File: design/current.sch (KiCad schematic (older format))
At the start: 4 parts

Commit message: Starting PIVI 2.0 * sch ready. * components in PCB placed.
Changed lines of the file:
@@
 AR Path="/548DF2C8/55B3BD79/55B231D6" Ref="R35"  Part="1"
 AR Path="/548DF2C8/55B3BD84/55B231D6" Ref="R38"  Part="1"
-F 0 "R23" V 3605 2675 50  0000 C CNN
+F 0 "R38" V 3605 2675 50  0000 C CNN
 F 1 "22R" V 3525 2675 50  0000 C CNN
 F 2 "Resistors_SMD:R_0603" V 3455 2675 30  0001 C CNN
@@
 AR Path="/548DF2C8/55B3BD79/55B23207" Ref="R36"  Part="1"
 AR Path="/548DF2C8/55B3BD84/55B23207" Ref="R39"  Part="1"
-F 0 "R24" V 4080 2675 50  0000 C CNN
+F 0 "R39" V 4080 2675 50  0000 C CNN
 F 1 "10K" V 4000 2675 50  0000 C CNN
 F 2 "Resistors_SMD:R_0603" V 3930 2675 30  0001 C CNN
@@
 AR Path="/548DF2C8/55B3BD79/55B23290" Ref="R37"  Part="1"
 AR Path="/548DF2C8/55B3BD84/55B23290" Ref="R40"  Part="1"
-F 0 "R25" V 4080 3175 50  0000 C CNN
+F 0 "R40" V 4080 3175 50  0000 C CNN
 F 1 "10K" V 4000 3175 50  0000 C CNN
 F 2 "Resistors_SMD:R_0603" V 3930 3175 30  0001 C CNN
@@
 AR Path="/548DF2C8/55B3BD79/55B232D0" Ref="C21"  Part="1"
 AR Path="/548DF2C8/55B3BD84/55B232D0" Ref="C22"  Part="1"
-F 0 "C17" H 3550 3275 50  0000 L CNN
+F 0 "C22" H 3550 3275 50  0000 L CNN
 F 1 "10uF" H 3550 3075 50  0000 L CNN
 F 2 "Capacitors_SMD:C_0805" H 3563 3025 30  0001 C CNN
@@
 Connection ~ 4000 2875
 $Comp
-L GND #PWR52
+L GND #PWR057
 U 1 1 55B23417
 P 3525 3375
-AR Path="/548DF2C8/55B266EE/55B23417" Ref="#PWR52"  Part="1"
-AR Path="/548DF2C8/55B3A3F6/55B23417" Ref="#PWR54"  Part="1"
-AR Path="/548DF2C8/55B3A74F/55B23417" Ref="#PWR56"  Part="1"
-AR Path="/548DF2C8/55B3BD6E/55B23417" Ref="#PWR58"  Part="1"
-AR Path="/548DF2C8/55B3BD79/55B23417" Ref="#PWR60"  Part="1"
-AR Path="/548DF2C8/55B3BD84/55B23417" Ref="#PWR62"  Part="1"
-F 0 "#PWR52" H 3525 3125 50  0001 C CNN
+AR Path="/548DF2C8/55B266EE/55B23417" Ref="#PWR057"  Part="1"
+AR Path="/548DF2C8/55B3A3F6/55B23417" Ref="#PWR059"  Part="1"
+AR Path="/548DF2C8/55B3A74F/55B23417" Ref="#PWR061"  Part="1"
+AR Path="/548DF2C8/55B3BD6E/55B23417" Ref="#PWR063"  Part="1"
+AR Path="/548DF2C8/55B3BD79/55B23417" Ref="#PWR065"  Part="1"
+AR Path="/548DF2C8/55B3BD84/55B23417" Ref="#PWR067"  Part="1"
+F 0 "#PWR067" H 3525 3125 50  0001 C CNN
 F 1 "GND" H 3525 3225 50  0000 C CNN
 F 2 "" H 3525 3375 60  0000 C CNN
@@
 	3525 3325 4000 3325
 $Comp
-L +3.3VADC #PWR53
+L +3.3VADC #PWR058
 U 1 1 55B9DD7E
 P 4000 2475
-AR Path="/548DF2C8/55B266EE/55B9DD7E" Ref="#PWR53"  Part="1"
-AR Path="/548DF2C8/55B3A3F6/55B9DD7E" Ref="#PWR55"  Part="1"
-AR Path="/548DF2C8/55B3A74F/55B9DD7E" Ref="#PWR57"  Part="1"
-AR Path="/548DF2C8/55B3BD6E/55B9DD7E" Ref="#PWR59"  Part="1"
-AR Path="/548DF2C8/55B3BD79/55B9DD7E" Ref="#PWR61"  Part="1"
-AR Path="/548DF2C8/55B3BD84/55B9DD7E" Ref="#PWR63"  Part="1"
-F 0 "#PWR53" H 4150 2425 50  0001 C CNN
+AR Path="/548DF2C8/55B266EE/55B9DD7E" Ref="#PWR058"  Part="1"
+AR Path="/548DF2C8/55B3A3F6/55B9DD7E" Ref="#PWR060"  Part="1"
+AR Path="/548DF2C8/55B3A74F/55B9DD7E" Ref="#PWR062"  Part="1"
+AR Path="/548DF2C8/55B3BD6E/55B9DD7E" Ref="#PWR064"  Part="1"
+AR Path="/548DF2C8/55B3BD79/55B9DD7E" Ref="#PWR066"  Part="1"
+AR Path="/548DF2C8/55B3BD84/55B9DD7E" Ref="#PWR068"  Part="1"
+F 0 "#PWR068" H 4150 2425 50  0001 C CNN
 F 1 "+3.3VADC" H 4000 2575 50  0000 C CNN
 F 2 "" H 4000 2475 60  0000 C CNN

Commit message: PCB routed + BOM complete
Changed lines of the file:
@@
 $Descr A4 11693 8268
 encoding utf-8
-Sheet 13 20
+Sheet 18 20
 Title "PIVI"
 Date "Mon 27 Jul 2015"
@@
 AR Path="/548DF2C8/55B3BD79/55B231D6" Ref="R35"  Part="1"
 AR Path="/548DF2C8/55B3BD84/55B231D6" Ref="R38"  Part="1"
-F 0 "R38" V 3605 2675 50  0000 C CNN
+F 0 "R23" V 3605 2675 50  0000 C CNN
 F 1 "22R" V 3525 2675 50  0000 C CNN
 F 2 "Resistors_SMD:R_0603" V 3455 2675 30  0001 C CNN
@@
 AR Path="/548DF2C8/55B3BD79/55B23207" Ref="R36"  Part="1"
 AR Path="/548DF2C8/55B3BD84/55B23207" Ref="R39"  Part="1"
-F 0 "R39" V 4080 2675 50  0000 C CNN
+F 0 "R24" V 4080 2675 50  0000 C CNN
 F 1 "10K" V 4000 2675 50  0000 C CNN
 F 2 "Resistors_SMD:R_0603" V 3930 2675 30  0001 C CNN
@@
 AR Path="/548DF2C8/55B3BD79/55B23290" Ref="R37"  Part="1"
 AR Path="/548DF2C8/55B3BD84/55B23290" Ref="R40"  Part="1"
-F 0 "R40" V 4080 3175 50  0000 C CNN
+F 0 "R25" V 4080 3175 50  0000 C CNN
 F 1 "10K" V 4000 3175 50  0000 C CNN
 F 2 "Resistors_SMD:R_0603" V 3930 3175 30  0001 C CNN
@@
 AR Path="/548DF2C8/55B3BD79/55B232D0" Ref="C21"  Part="1"
 AR Path="/548DF2C8/55B3BD84/55B232D0" Ref="C22"  Part="1"
-F 0 "C22" H 3550 3275 50  0000 L CNN
+F 0 "C17" H 3550 3275 50  0000 L CNN
 F 1 "10uF" H 3550 3075 50  0000 L CNN
 F 2 "Capacitors_SMD:C_0805" H 3563 3025 30  0001 C CNN
@@
 AR Path="/548DF2C8/55B3BD79/55B23417" Ref="#PWR065"  Part="1"
 AR Path="/548DF2C8/55B3BD84/55B23417" Ref="#PWR067"  Part="1"
-F 0 "#PWR067" H 3525 3125 50  0001 C CNN
+F 0 "#PWR057" H 3525 3125 50  0001 C CNN
 F 1 "GND" H 3525 3225 50  0000 C CNN
 F 2 "" H 3525 3375 60  0000 C CNN
@@
 AR Path="/548DF2C8/55B3BD79/55B9DD7E" Ref="#PWR066"  Part="1"
 AR Path="/548DF2C8/55B3BD84/55B9DD7E" Ref="#PWR068"  Part="1"
-F 0 "#PWR068" H 4150 2425 50  0001 C CNN
+F 0 "#PWR058" H 4150 2425 50  0001 C CNN
 F 1 "+3.3VADC" H 4000 2575 50  0000 C CNN
 F 2 "" H 4000 2475 60  0000 C CNN

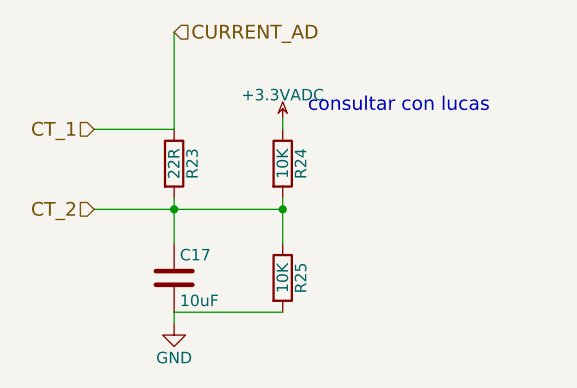
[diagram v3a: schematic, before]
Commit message: Fix #7, Fix #8, Fix #9, Fix #10, Fix #11
Several fixes improvements:
* Fix #7: Add 2mm idle to each side of the connector.
* Fix #8: Add 0.25mm to each side of the connector.
* Fix #9: Mirror component. Checked with the datasheet.
* Fix #10: correct label name.
* Fix #11: Changed the terminal block for one with a better mouting system.

Also check the Raspberry pi 20 pin header. It is place in the correct position.
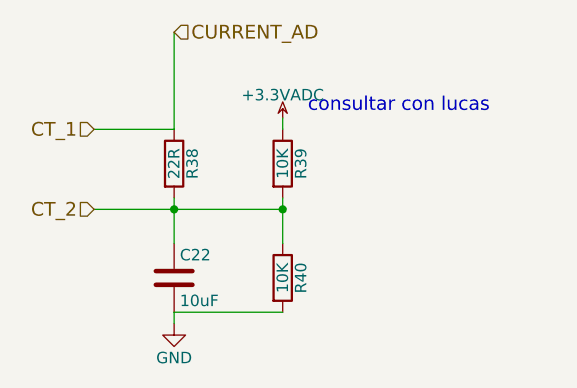
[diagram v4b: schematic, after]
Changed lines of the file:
@@
 AR Path="/548DF2C8/55B3BD79/55B231D6" Ref="R35"  Part="1"
 AR Path="/548DF2C8/55B3BD84/55B231D6" Ref="R38"  Part="1"
-F 0 "R23" V 3605 2675 50  0000 C CNN
+F 0 "R38" V 3605 2675 50  0000 C CNN
 F 1 "22R" V 3525 2675 50  0000 C CNN
 F 2 "Resistors_SMD:R_0603" V 3455 2675 30  0001 C CNN
@@
 AR Path="/548DF2C8/55B3BD79/55B23207" Ref="R36"  Part="1"
 AR Path="/548DF2C8/55B3BD84/55B23207" Ref="R39"  Part="1"
-F 0 "R24" V 4080 2675 50  0000 C CNN
+F 0 "R39" V 4080 2675 50  0000 C CNN
 F 1 "10K" V 4000 2675 50  0000 C CNN
 F 2 "Resistors_SMD:R_0603" V 3930 2675 30  0001 C CNN
@@
 AR Path="/548DF2C8/55B3BD79/55B23290" Ref="R37"  Part="1"
 AR Path="/548DF2C8/55B3BD84/55B23290" Ref="R40"  Part="1"
-F 0 "R25" V 4080 3175 50  0000 C CNN
+F 0 "R40" V 4080 3175 50  0000 C CNN
 F 1 "10K" V 4000 3175 50  0000 C CNN
 F 2 "Resistors_SMD:R_0603" V 3930 3175 30  0001 C CNN
@@
 AR Path="/548DF2C8/55B3BD79/55B232D0" Ref="C21"  Part="1"
 AR Path="/548DF2C8/55B3BD84/55B232D0" Ref="C22"  Part="1"
-F 0 "C17" H 3550 3275 50  0000 L CNN
+F 0 "C22" H 3550 3275 50  0000 L CNN
 F 1 "10uF" H 3550 3075 50  0000 L CNN
 F 2 "Capacitors_SMD:C_0805" H 3563 3025 30  0001 C CNN
